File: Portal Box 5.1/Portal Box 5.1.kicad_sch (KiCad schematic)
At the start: 81 parts, among them J1 Conn_01x04, J2 Conn_01x04, J3 Conn_01x02, J4 732-6001-1-ND, J5 RFID-RC522, J6 609-87520-0010ALFCT-ND, J7 2073-USB4105-GF-ACT-ND, J8 A 14-LC-TT, K1 PR28-5V-360-1A-E, K2 DIP05-2A72-21L, Q1 NTR5103NT1G, Q2 NTR5103NT1G, SW1 141-TL3336AF160QCT-ND, U1 448-TLE4971A050T5UE0001XUMA1C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, U2 497-5026-1-ND, U3 ESP32-S3-DEVKITC-1-N8R8-OFFIC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, U4 497-5026-1-ND, U5 AP7363-33D-13

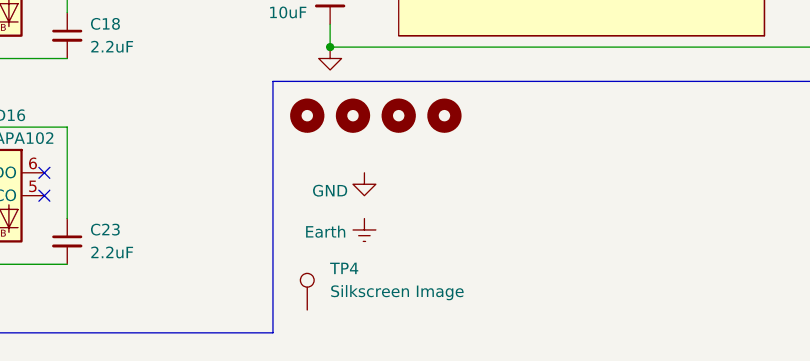
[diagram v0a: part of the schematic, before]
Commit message: fix drc errors and remove tp4 reference
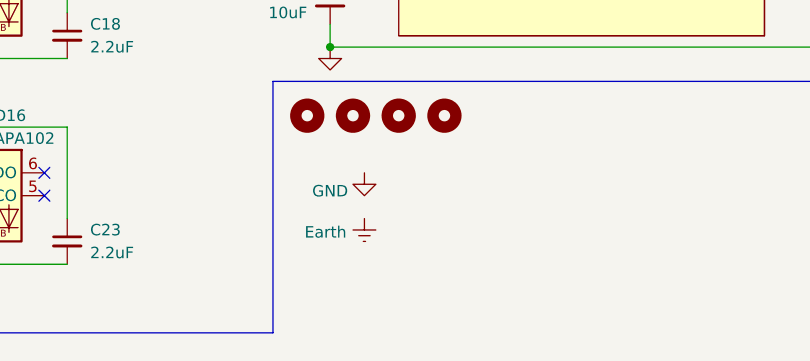
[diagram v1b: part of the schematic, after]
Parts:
- removed TP4: Silkscreen Image, portalbox:MakerELogoSilkscreen, symbol Connector:TestPoint
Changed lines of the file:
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@@
-	)
-	(symbol
-		(lib_id "Connector:TestPoint")
-		(at 170.18 240.03 0)
-		(unit 1)
-		(exclude_from_sim no)
-		(in_bom yes)
-		(on_board yes)
-		(dnp no)
-		(fields_autoplaced yes)
-		(property "Reference" "TP4"
-			(at 172.72 235.4579 0)
-			(effects
-				(font
-					(size 1.27 1.27)
-				)
-				(justify left)
-			)
-		)
-		(property "Value" "Silkscreen Image"
-			(at 172.72 237.9979 0)
-			(effects
-				(font
-					(size 1.27 1.27)
-				)
-				(justify left)
-			)
-		)
-		(property "Footprint" "portalbox:MakerELogoSilkscreen"
-			(at 175.26 240.03 0)
-			(effects
-				(font
-					(size 1.27 1.27)
-				)
-				(hide yes)
-			)
-		)
-		(property "Datasheet" "~"
-			(at 175.26 240.03 0)
-			(effects
-				(font
-					(size 1.27 1.27)
-				)
-				(hide yes)
-			)
-		)
-		(property "Description" "test point"
-			(at 170.18 240.03 0)
-			(effects
-				(font
-					(size 1.27 1.27)
-				)
-				(hide yes)
-			)
-		)
-		(pin "1"
-		)
-		(instances
-			(project ""
-				(path "/ba768599-a152-4e41-90f8-f7ba0e92f17c"
-					(reference "TP4")
-					(unit 1)
-				)
-			)
-		)
 	)
 	(symbol
